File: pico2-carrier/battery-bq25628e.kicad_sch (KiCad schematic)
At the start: 17 parts, among them IC4 BQ25628ERYKR

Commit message: start work on PCB
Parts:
- removed R6, R7: R, Resistor_SMD:R_0402_1005Metric, symbol Device:R
- BT1: footprint Jumper:SolderJumper-2_P1.3mm_Open_Pad1.0x1.5mm -> Connector_JST:JST_PH_B2B-PH-K_1x02_P2.00mm_Vertical
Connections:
- net BAT is gone; now on net BAT+: IC4.8 (BAT)
- net ~{PG}: now reaches D1.1 (K), IC4.3 (~{PG})
- no-connect marks 1 -> 3
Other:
- note added: ""The TS pin may be left floating if TS_IGNORE is set to 1" - BQ25628E datasheet 8.3.5.4"
- note removed: "Bat doesn't have thermistor Assuming hard-wiring will be fine"

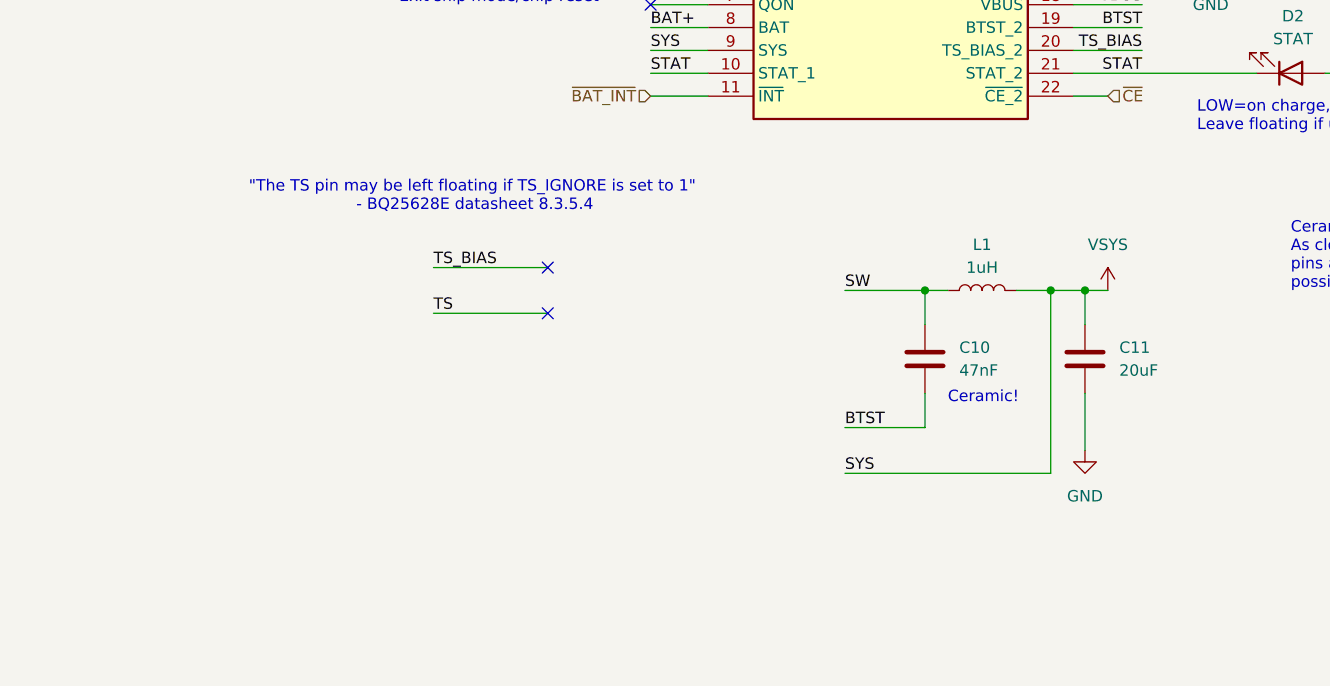
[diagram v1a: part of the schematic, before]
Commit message: add PFET to VSYS input
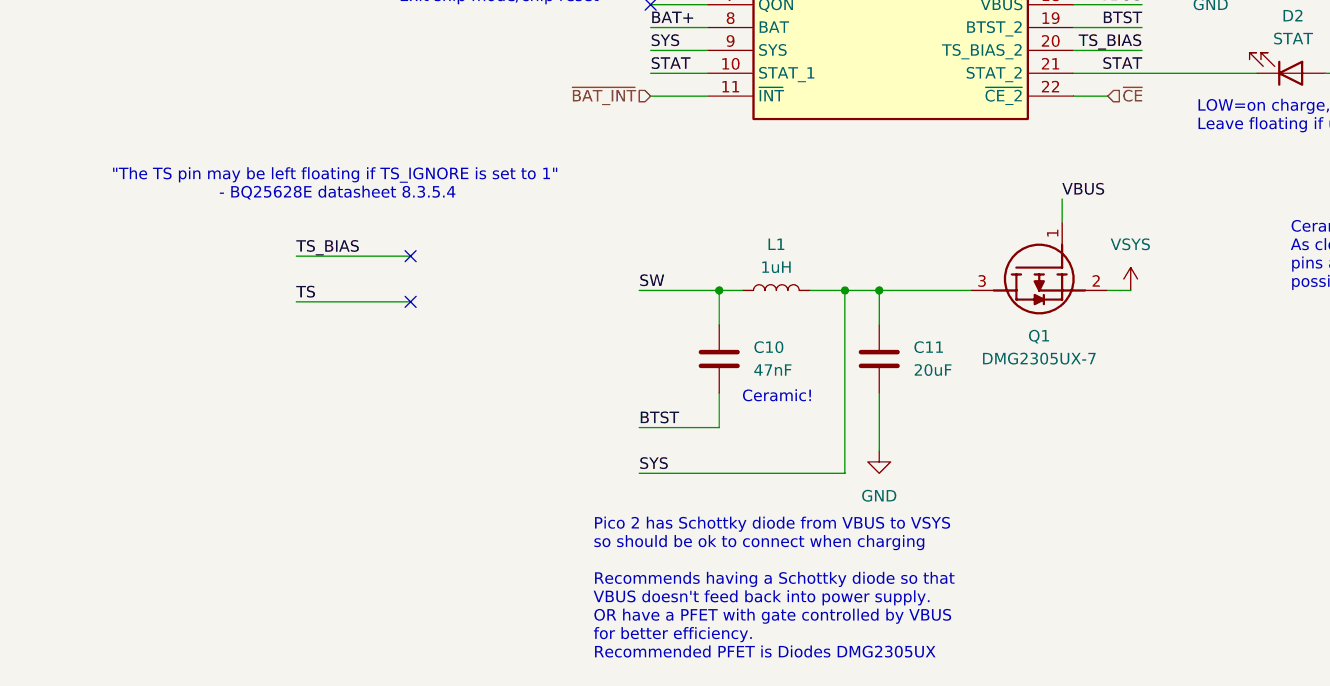
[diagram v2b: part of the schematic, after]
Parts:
- added Q1: DMG2305UX-7, SOT96P240X115-3N, symbol SamacSys_Parts:DMG2305UX-7
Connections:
- net VBUS: now also Q1.1 (G)
- net VSYS: now also Q1.2 (S); no longer C11.1, IC4.9 (SYS), L1.2
- new net SYS: C11.1, IC4.9 (SYS), L1.2, Q1.3 (D)
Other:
- note added: "Pico 2 has Schottky diode from VBUS to VSYS so should be ok to connect when charging Recommends having a Schottky diode so that VBUS doesn't feed back into power supply. OR have a PFET with gate controlled by VBUS for better efficiency. Recommended PFET is Diodes DMG2305UX"
- moved on the sheet: C10, C11, L1

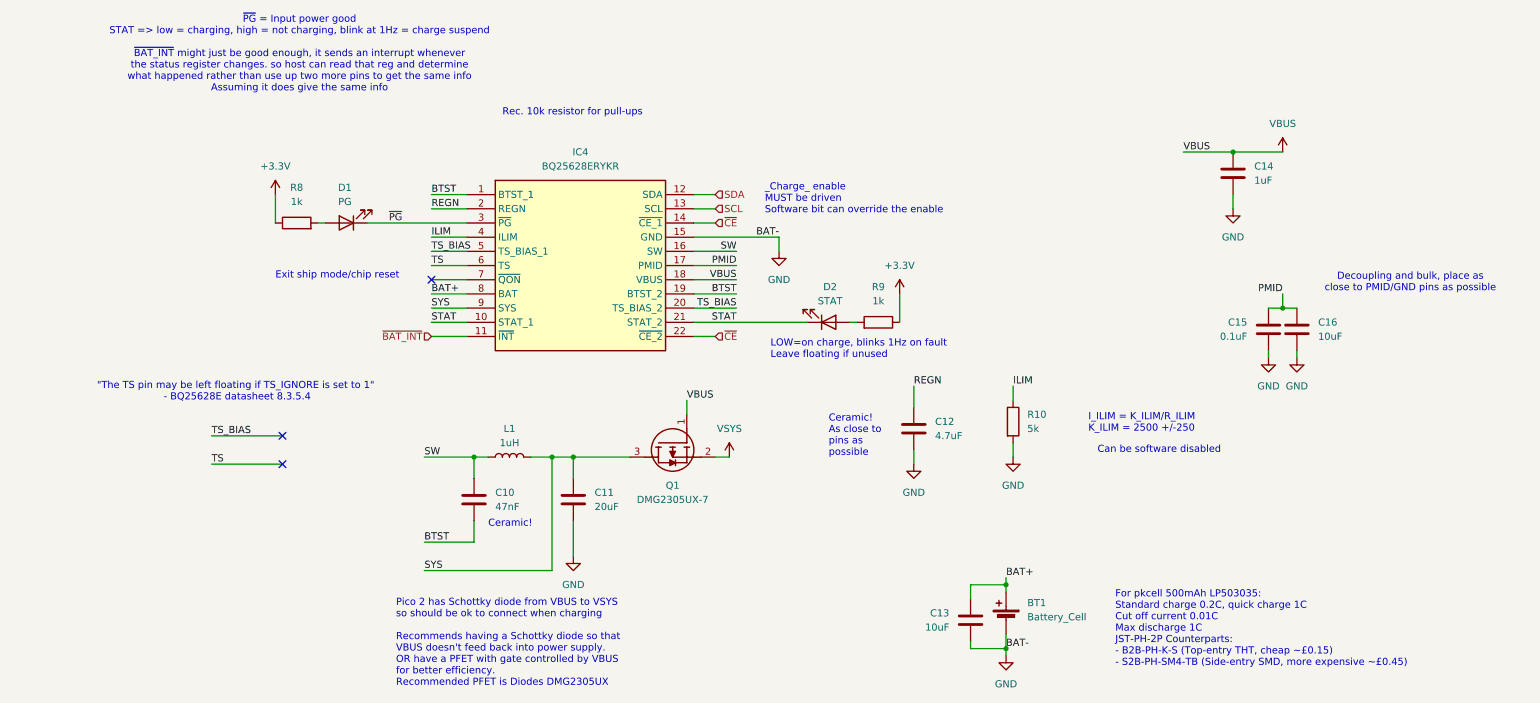
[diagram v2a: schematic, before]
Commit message: carrier: add some test points and default jumper connections
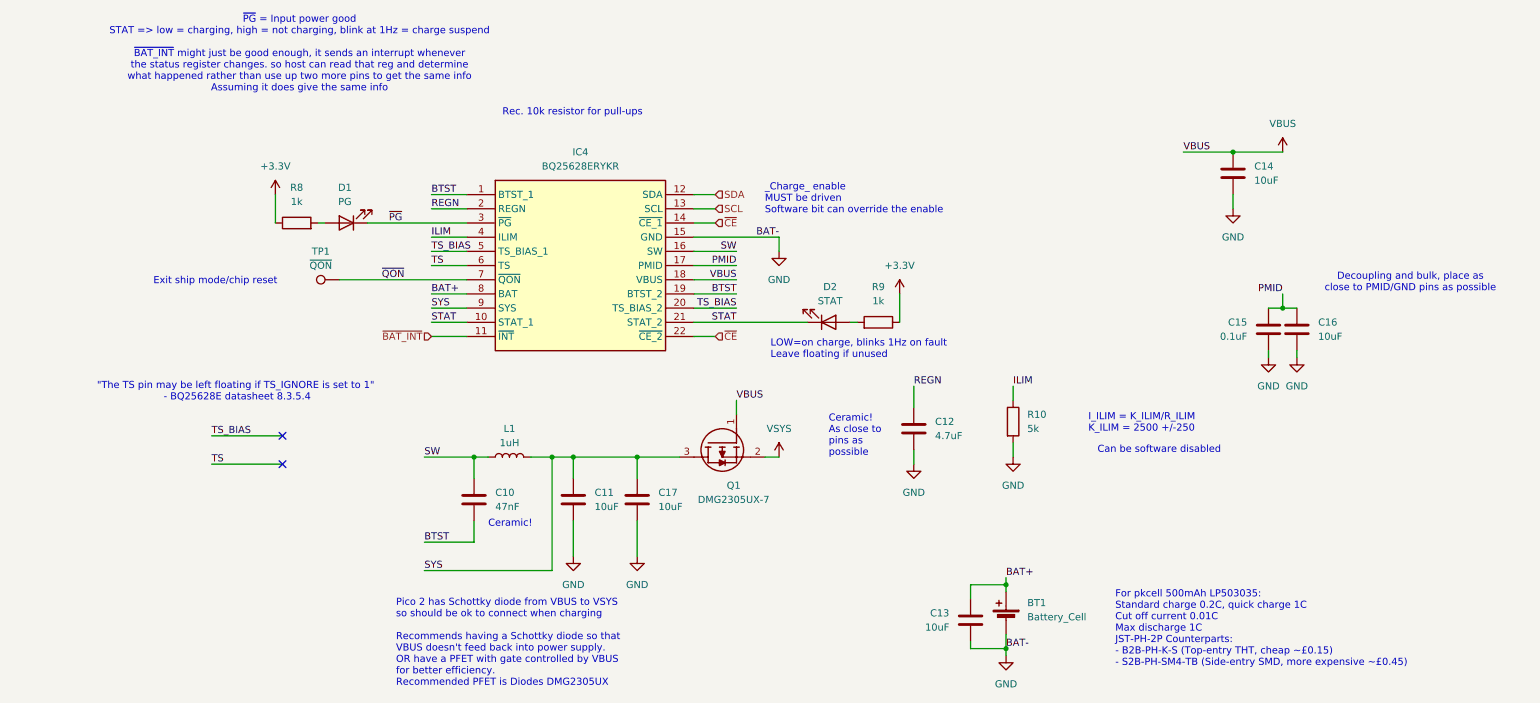
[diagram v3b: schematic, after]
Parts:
- added C17: 10uF, Capacitor_SMD:C_0402_1005Metric, symbol Device:C
- added TP1: ~{QON}, Connector_PinHeader_2.54mm:PinHeader_1x01_P2.54mm_Vertical, symbol Connector:TestPoint
- C11: value 20uF -> 10uF
- C14: value 1uF -> 10uF
- Q1: footprint SOT96P240X115-3N -> SamacsysParts:SOT96P240X115-3N
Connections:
- net GND: now also C17.2
- net SYS: now also C17.1
- net ~{QON}: now reaches IC4.7 (~{QON})
- net ~{QON}: now also TP1.1
- no-connect marks 3 -> 2
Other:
- moved on the sheet: Q1

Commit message: carrier: add 3.3V zone, start tidying buttons, update caps to 0603
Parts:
- C10, C11, C12, C13, C14, C16, C17: footprint Capacitor_SMD:C_0402_1005Metric -> Capacitor_SMD:C_0603_1608Metric
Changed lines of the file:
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@@
 			)
 		)
-		(property "Footprint" "Capacitor_SMD:C_0402_1005Metric"
+		(property "Footprint" "Capacitor_SMD:C_0603_1608Metric"
 			(at 237.1852 85.09 0)
 			(effects
@@
 			)
 		)
-		(property "Footprint" "Capacitor_SMD:C_0402_1005Metric"
+		(property "Footprint" "Capacitor_SMD:C_0603_1608Metric"
 			(at 178.7652 137.16 0)
 			(effects
@@
 			)
 		)
-		(property "Footprint" "Capacitor_SMD:C_0402_1005Metric"
+		(property "Footprint" "Capacitor_SMD:C_0603_1608Metric"
 			(at 89.8652 115.57 0)
 			(effects
@@
 			)
 		)
-		(property "Footprint" "Capacitor_SMD:C_0402_1005Metric"
+		(property "Footprint" "Capacitor_SMD:C_0603_1608Metric"
 			(at 119.0752 115.57 0)
 			(effects
@@
 			)
 		)
-		(property "Footprint" "Capacitor_SMD:C_0402_1005Metric"
+		(property "Footprint" "Capacitor_SMD:C_0603_1608Metric"
 			(at 107.6452 115.57 0)
 			(effects
@@
 			)
 		)
-		(property "Footprint" "Capacitor_SMD:C_0402_1005Metric"
+		(property "Footprint" "Capacitor_SMD:C_0603_1608Metric"
 			(at 168.6052 102.87 0)
 			(effects
@@
 			)
 		)
-		(property "Footprint" "Capacitor_SMD:C_0402_1005Metric"
+		(property "Footprint" "Capacitor_SMD:C_0603_1608Metric"
 			(at 225.7552 57.15 0)
 			(effects

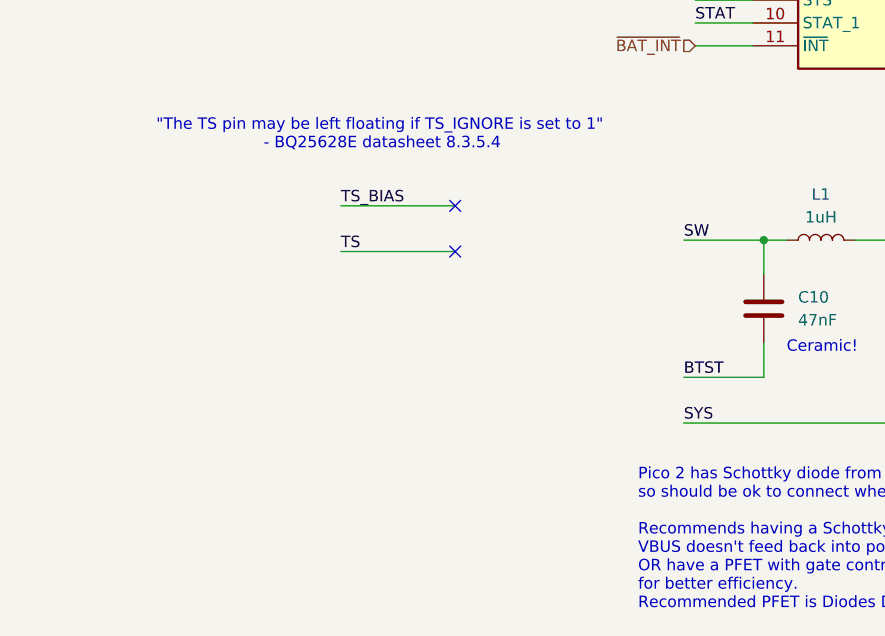
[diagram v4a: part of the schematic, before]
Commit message: carrier: update PMIC layout and button filters
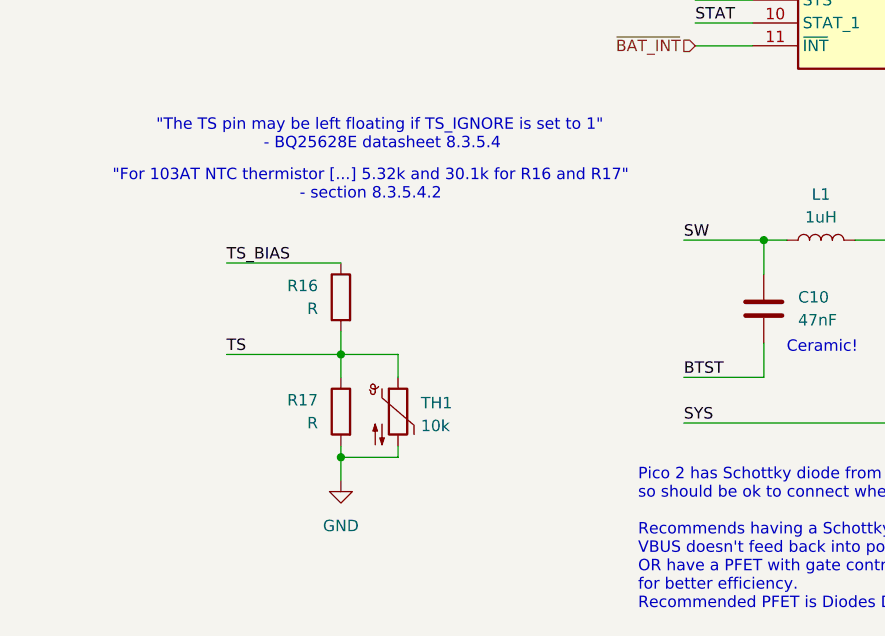
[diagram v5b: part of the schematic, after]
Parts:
- added R16, R17: R, Resistor_SMD:R_0402_1005Metric, symbol Device:R
- added TH1: 10k, Resistor_SMD:R_0603_1608Metric, symbol Device:Thermistor_NTC
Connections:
- net GND: now also R17.2, TH1.2
- net TS: now also R16.2, R17.1, TH1.1
- net TS_BIAS: now also R16.1
- no-connect marks 2 -> 0
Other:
- note added: ""For 103AT NTC thermistor [...] 5.32k and 30.1k for R16 and R17" - section 8.3.5.4.2"

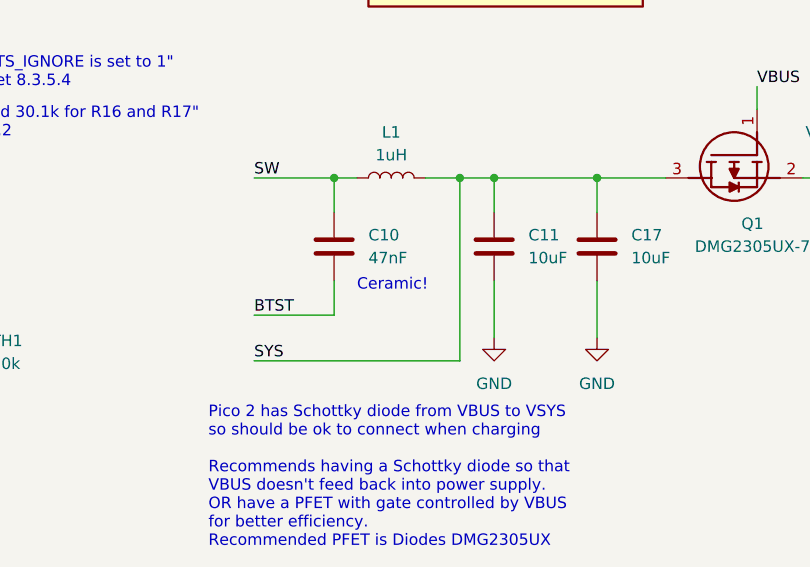
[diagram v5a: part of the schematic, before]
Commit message: carrier: add notes on capacitors
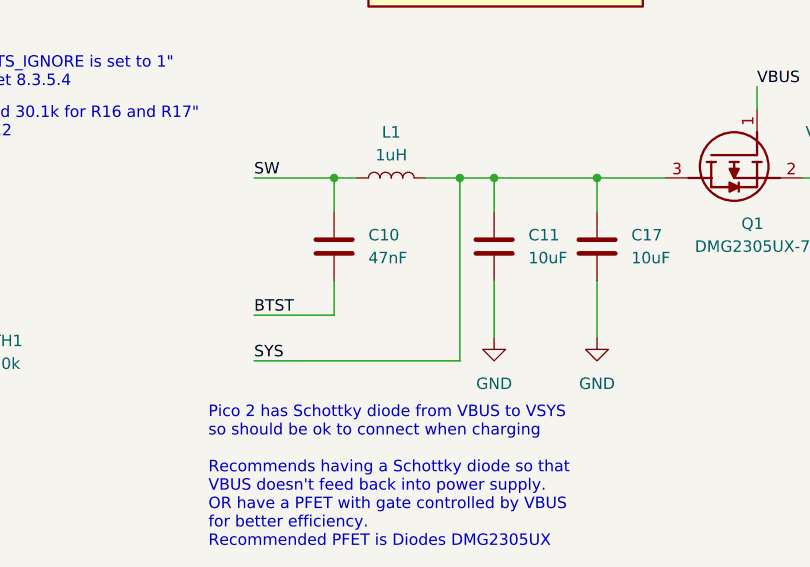
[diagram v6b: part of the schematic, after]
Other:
- note removed: "Ceramic!"
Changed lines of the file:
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@@
-		)
-	)
-	(text "Ceramic!"
-		(exclude_from_sim no)
-		(at 91.44 116.84 0)
-		(effects
-			(font
-				(size 1.27 1.27)
-			)
-			(justify left bottom)
 		)
 	)
